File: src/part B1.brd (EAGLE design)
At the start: 41 x 75.5 mm, 0 parts

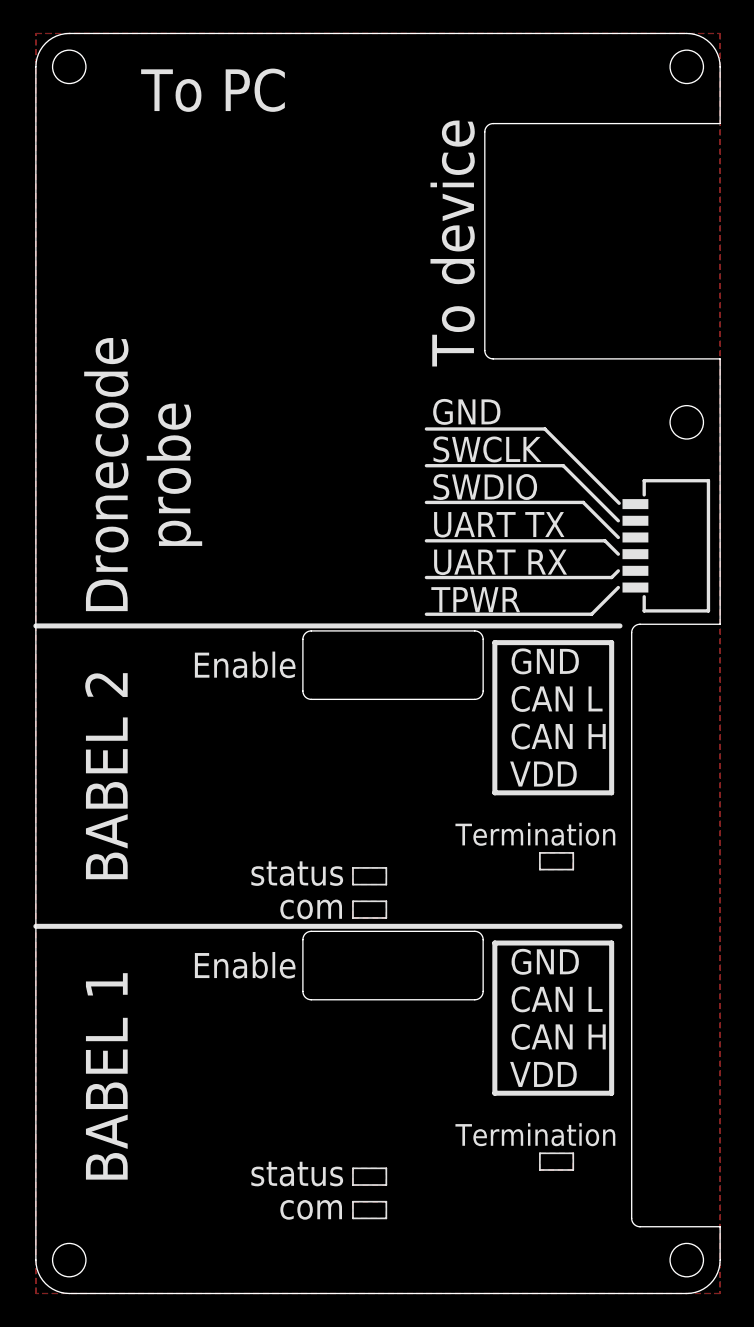
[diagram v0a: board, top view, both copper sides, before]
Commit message: Redoing past changes and new fixes (#20)
* fixed mosfet Q2

* fixed switch label in top board

* removed unnecessary assembly variant
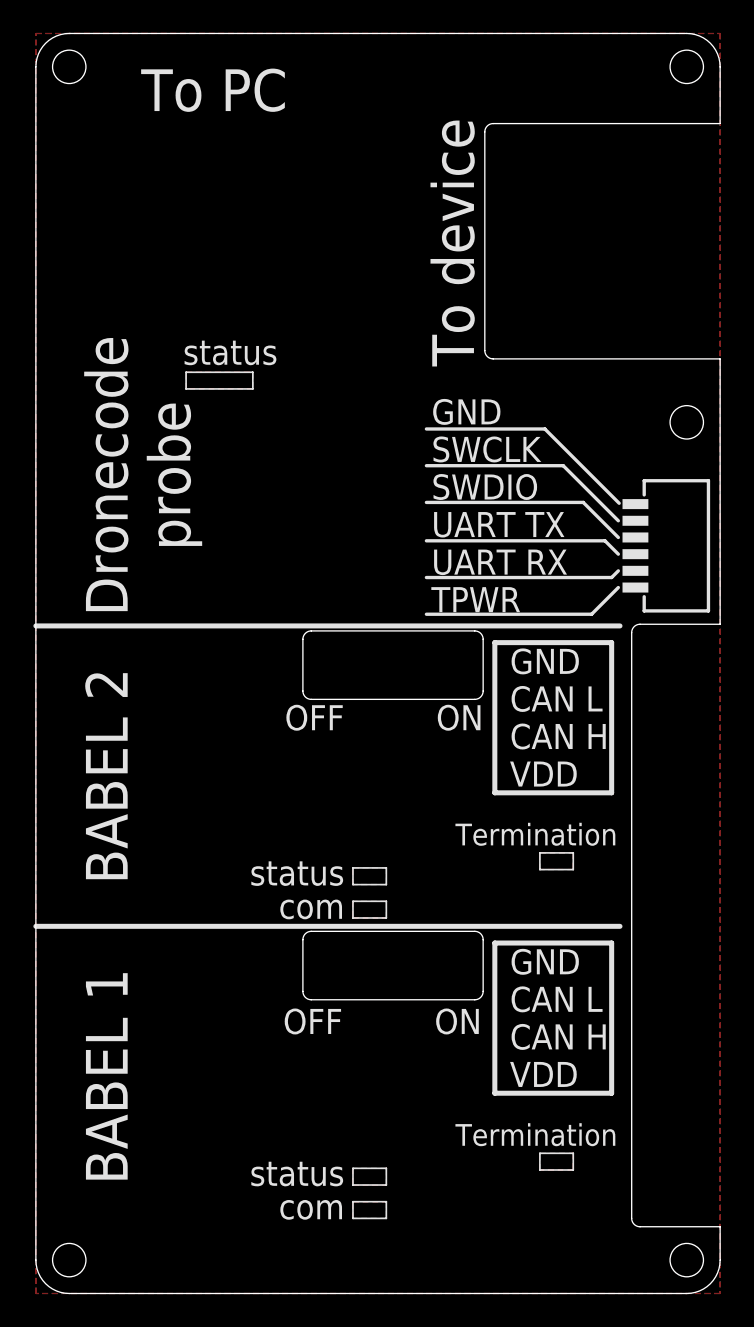
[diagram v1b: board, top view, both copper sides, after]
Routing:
- added copper zone on layer 1, net S$7
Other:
- board text added: "OFF"
- board text added: "ON"
- board text removed: "Enable"

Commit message: Revert "Fixed mosfet Q2 from both babel, fixes #6 (#12)"
This reverts commit d39d7e4d46531cf5480a8d684ba2b4b43b92db19.
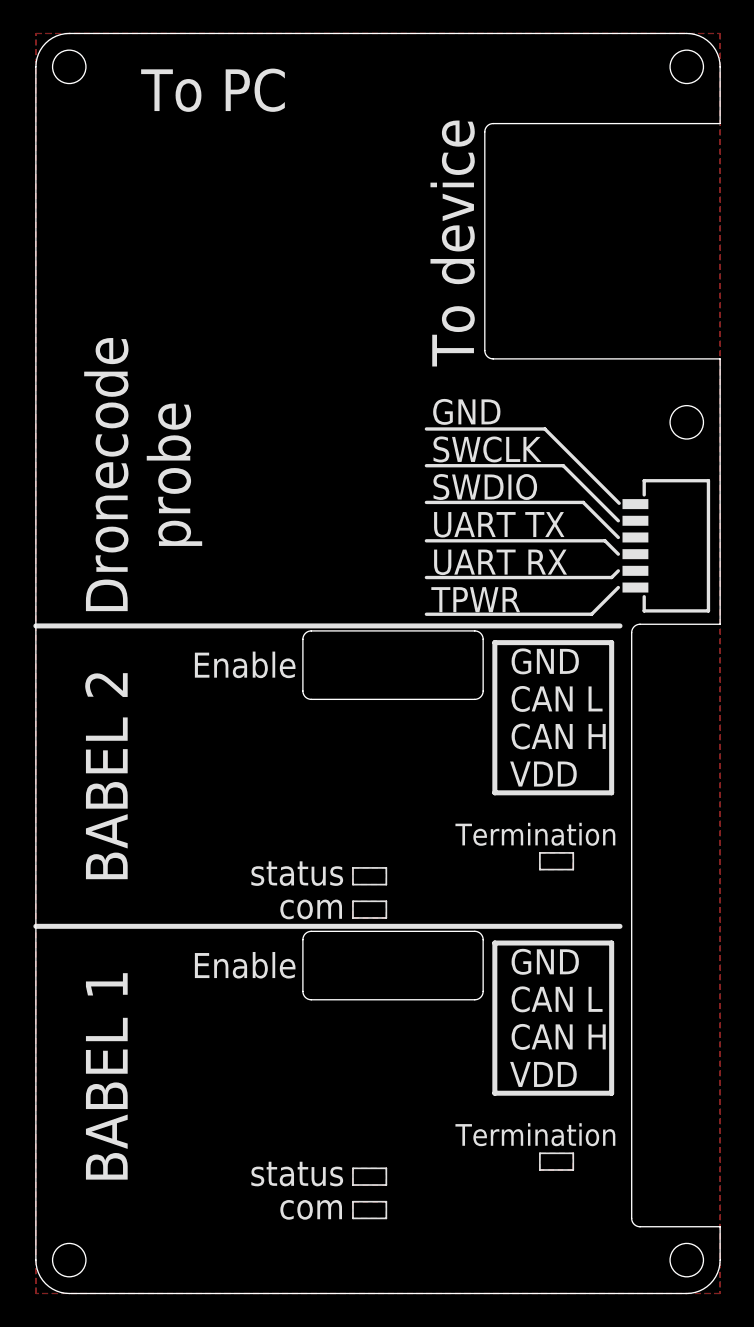
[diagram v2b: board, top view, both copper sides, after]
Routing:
- removed copper zone on layer 1, net S$7
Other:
- board text added: "Enable"
- board text removed: "OFF"
- board text removed: "ON"
